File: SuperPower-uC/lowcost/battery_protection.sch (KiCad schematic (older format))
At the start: 0 parts

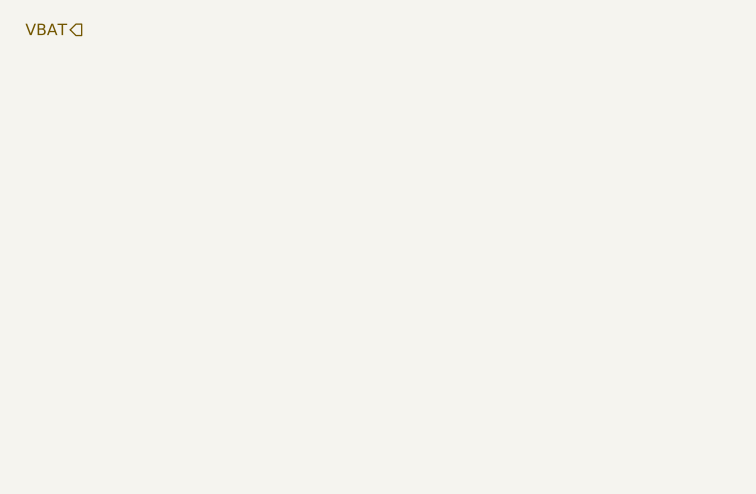
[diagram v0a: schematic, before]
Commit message: added battery protection schematic
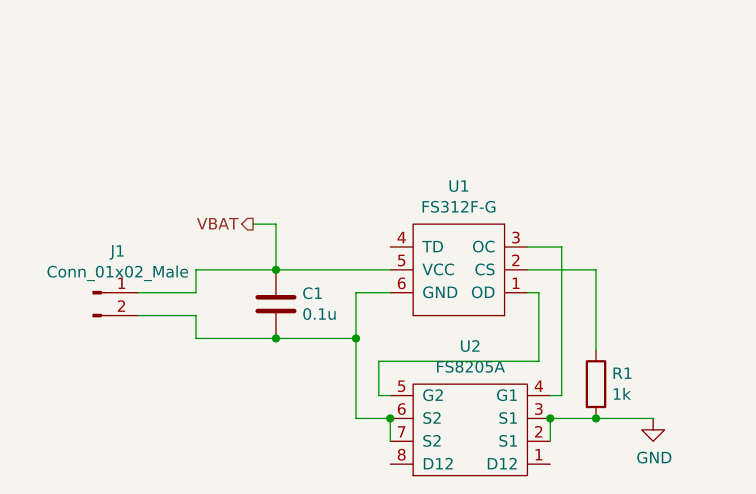
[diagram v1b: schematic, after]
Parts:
- added C1: 0.1u, Capacitor_SMD:C_0603_1608Metric_Pad1.05x0.95mm_HandSolder, symbol Device:C
- added J1: Conn_01x02_Male, Connector_JST:JST_EH_S2B-EH_1x02_P2.50mm_Horizontal, symbol Connector:Conn_01x02_Male
- added R1: 1k, Resistor_SMD:R_0603_1608Metric_Pad1.05x0.95mm_HandSolder, symbol Device:R
- added U1: FS312F-G, Package_TO_SOT_SMD:SOT-23-6_Handsoldering, symbol FS312F-G:FS312F-G
- added U2: FS8205A, Package_SO:TSSOP-8_4.4x3mm_P0.65mm, symbol FS8205A:FS8205A
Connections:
- net VBAT: now also C1.1, J1.1 (Pin_1), U1.5 (VCC)
- new net: U1.1 (OD), U2.5 (G2)
- new net: R1.1, U1.2 (CS)
- new net: U1.3 (OC), U2.4 (G1)
- new net: C1.2, J1.2 (Pin_2), U1.6 (GND), U2.6 (S2), U2.7 (S2)
- new net GND: R1.2, U2.2 (S1), U2.3 (S1)
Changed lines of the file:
@@
 Comment4 ""
 $EndDescr
-Text HLabel 1250 1350 0    50   Output ~ 0
+Text HLabel 2000 2200 0    50   Output ~ 0
 VBAT
+$Comp
+L FS312F-G:FS312F-G U1
+U 1 1 5F7C508D
+P 2900 2500
+F 0 "U1" H 2900 2035 50  0000 C CNN
+F 1 "FS312F-G" H 2900 2126 50  0000 C CNN
+F 2 "Package_TO_SOT_SMD:SOT-23-6_Handsoldering" H 3000 2950 50  0001 C CNN
+F 3 "https://www.ic-fortune.com/upload/Download/FS312F-G-DS-12_EN.pdf" H 2900 2250 50  0001 C CNN
+F 4 " C82736" H 2900 2500 50  0001 C CNN "LCSC"
+	1    2900 2500
+	-1   0    0    1
+$EndComp
+$Comp
+L FS8205A:FS8205A U2
+U 1 1 5F7C57B0
+P 2950 3150
+F 0 "U2" H 2950 2735 50  0000 C CNN
+F 1 "FS8205A" H 2950 2826 50  0000 C CNN
+F 2 "Package_SO:TSSOP-8_4.4x3mm_P0.65mm" H 2950 3450 50  0001 C CNN
+F 3 "https://www.ic-fortune.com/upload/Download/FS8205A-DS-12_EN.pdf" H 2950 3450 50  0001 C CNN
+F 4 " C16052" H 2950 3150 50  0001 C CNN "LCSC"
+	1    2950 3150
+	-1   0    0    1
+$EndComp
+Wire Wire Line
+	2600 2950 2550 2950
+Wire Wire Line
+	2550 2950 2550 2800
+Wire Wire Line
+	2550 2800 3250 2800
+Wire Wire Line
+	3250 2800 3250 2500
+Wire Wire Line
+	3250 2500 3200 2500
+Wire Wire Line
+	3200 2300 3350 2300
+Wire Wire Line
+	3350 2300 3350 2950
+Wire Wire Line
+	3350 2950 3300 2950
+Wire Wire Line
+	2600 3150 2600 3050
+Wire Wire Line
+	2600 3050 2450 3050
+Wire Wire Line
+	2450 2500 2600 2500
+Connection ~ 2600 3050
+Wire Wire Line
+	2600 2400 2100 2400
+Wire Wire Line
+	2450 2700 2100 2700
+Wire Wire Line
+	2000 2200 2100 2200
+Wire Wire Line
+	2100 2200 2100 2400
+Connection ~ 2100 2400
+Wire Wire Line
+	2100 2400 1750 2400
+$Comp
+L Device:R R1
+U 1 1 5F7CFA8D
+P 3500 2900
+F 0 "R1" H 3570 2946 50  0000 L CNN
+F 1 "1k" H 3570 2855 50  0000 L CNN
+F 2 "Resistor_SMD:R_0603_1608Metric_Pad1.05x0.95mm_HandSolder" V 3430 2900 50  0001 C CNN
+F 3 "~" H 3500 2900 50  0001 C CNN
+F 4 "C21190" H 3500 2900 50  0001 C CNN "LCSC"
+	1    3500 2900
+	1    0    0    -1
+$EndComp
+$Comp
+L Device:C C1
+U 1 1 5F7D0298
+P 2100 2550
+F 0 "C1" H 2215 2596 50  0000 L CNN
+F 1 "0.1u" H 2215 2505 50  0000 L CNN
+F 2 "Capacitor_SMD:C_0603_1608Metric_Pad1.05x0.95mm_HandSolder" H 2138 2400 50  0001 C CNN
+F 3 "~" H 2100 2550 50  0001 C CNN
+F 4 "C14858" H 2100 2550 50  0001 C CNN "LCSC"
+	1    2100 2550
+	1    0    0    -1
+$EndComp
+Connection ~ 2100 2700
+Wire Wire Line
+	2100 2700 1750 2700
+Connection ~ 2450 2700
+Wire Wire Line
+	2450 2700 2450 2500
+Wire Wire Line
+	2450 2700 2450 3050
+Wire Wire Line
+	3500 3050 3300 3050
+Wire Wire Line
+	3300 3150 3300 3050
+Connection ~ 3300 3050
+Wire Wire Line
+	3500 2750 3500 2400
+Wire Wire Line
+	3500 2400 3200 2400
+$Comp
+L power:GND #PWR?
+U 1 1 5F7D3A76
+P 3750 3050
+F 0 "#PWR?" H 3750 2800 50  0001 C CNN
+F 1 "GND" H 3755 2877 50  0000 C CNN
+F 2 "" H 3750 3050 50  0001 C CNN
+F 3 "" H 3750 3050 50  0001 C CNN
+	1    3750 3050
+	1    0    0    -1
+$EndComp
+Wire Wire Line
+	3750 3050 3500 3050
+Connection ~ 3500 3050
+$Comp
+L Connector:Conn_01x02_Male J1
+U 1 1 5F7D5382
+P 1300 2500
+F 0 "J1" H 1408 2681 50  0000 C CNN
+F 1 "Conn_01x02_Male" H 1408 2590 50  0000 C CNN
+F 2 "Connector_JST:JST_EH_S2B-EH_1x02_P2.50mm_Horizontal" H 1300 2500 50  0001 C CNN
+F 3 "~" H 1300 2500 50  0001 C CNN
+F 4 "C157931" H 1300 2500 50  0001 C CNN "LCSC"
+	1    1300 2500
+	1    0    0    -1
+$EndComp
+Wire Wire Line
+	1750 2400 1750 2500
+Wire Wire Line
+	1750 2500 1500 2500
+Wire Wire Line
+	1500 2600 1750 2600
+Wire Wire Line
+	1750 2600 1750 2700
 $EndSCHEMATC

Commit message: int pins and charging module
added Interrupt pins to the main sheet and finished the charging module sub sheet (with charger, fuel Gauge and power on int)
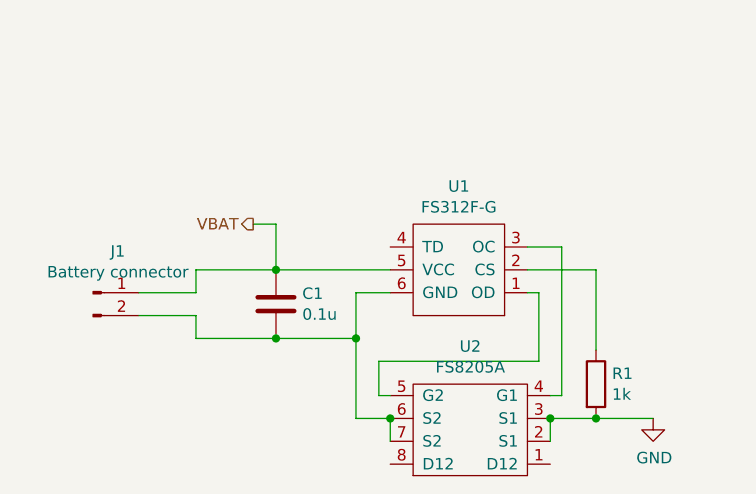
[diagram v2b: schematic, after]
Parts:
- J1: value Conn_01x02_Male -> Battery connector
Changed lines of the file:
@@
 P 1300 2500
 F 0 "J1" H 1408 2681 50  0000 C CNN
-F 1 "Conn_01x02_Male" H 1408 2590 50  0000 C CNN
+F 1 "Battery connector" H 1408 2590 50  0000 C CNN
 F 2 "Connector_JST:JST_EH_S2B-EH_1x02_P2.50mm_Horizontal" H 1300 2500 50  0001 C CNN
 F 3 "~" H 1300 2500 50  0001 C CNN

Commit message: added ftdi and some cleanup
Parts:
- U1: LCSC C82736 -> C82736
- U2: LCSC C16052 -> C16052
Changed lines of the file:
@@
 F 2 "Package_TO_SOT_SMD:SOT-23-6_Handsoldering" H 3000 2950 50  0001 C CNN
 F 3 "https://www.ic-fortune.com/upload/Download/FS312F-G-DS-12_EN.pdf" H 2900 2250 50  0001 C CNN
-F 4 " C82736" H 2900 2500 50  0001 C CNN "LCSC"
+F 4 "C82736" H 2900 2500 50  0001 C CNN "LCSC"
 	1    2900 2500
 	-1   0    0    1
@@
 F 2 "Package_SO:TSSOP-8_4.4x3mm_P0.65mm" H 2950 3450 50  0001 C CNN
 F 3 "https://www.ic-fortune.com/upload/Download/FS8205A-DS-12_EN.pdf" H 2950 3450 50  0001 C CNN
-F 4 " C16052" H 2950 3150 50  0001 C CNN "LCSC"
+F 4 "C16052" H 2950 3150 50  0001 C CNN "LCSC"
 	1    2950 3150
 	-1   0    0    1
@@
 F 1 "Battery connector" H 1408 2590 50  0000 C CNN
 F 2 "Connector_JST:JST_EH_S2B-EH_1x02_P2.50mm_Horizontal" H 1300 2500 50  0001 C CNN
-F 3 "~" H 1300 2500 50  0001 C CNN
+F 3 "https://datasheet.lcsc.com/szlcsc/1811051822_JST-Sales-America-S2B-XH-A-LF-SN_C157931.pdf" H 1300 2500 50  0001 C CNN
 F 4 "C157931" H 1300 2500 50  0001 C CNN "LCSC"
 	1    1300 2500

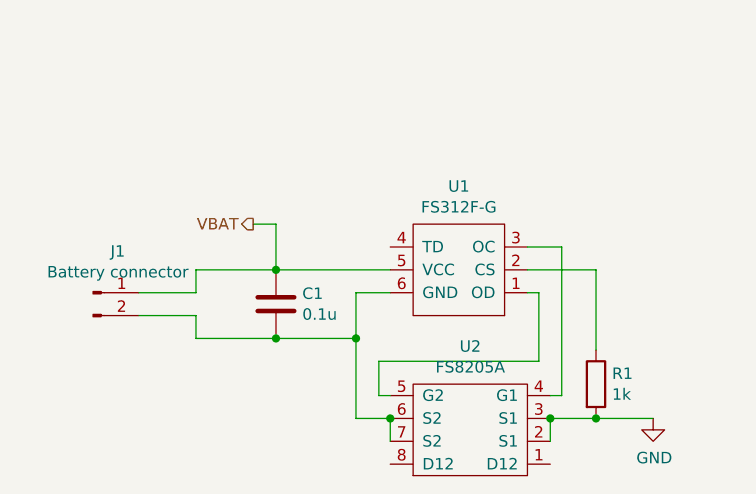
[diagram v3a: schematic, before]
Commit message: fixed mentioned issues and swapped micro usb with usb c
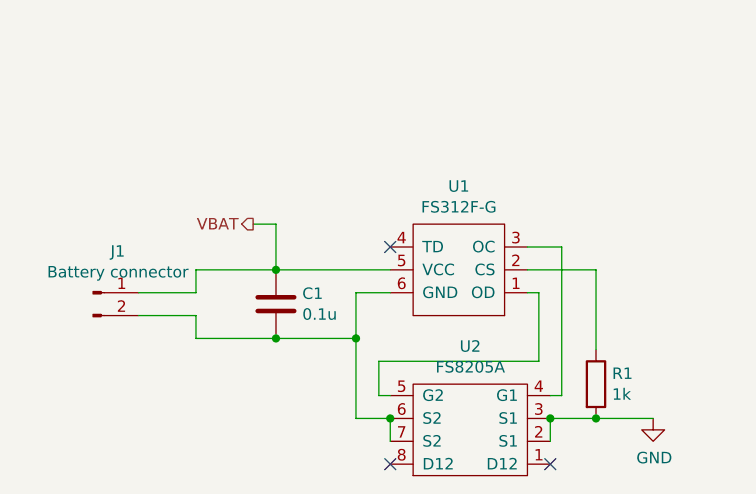
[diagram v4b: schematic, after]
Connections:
- no-connect marks 0 -> 3
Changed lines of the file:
@@
 Wire Wire Line
 	1750 2600 1750 2700
+NoConn ~ 2600 3250
+NoConn ~ 3300 3250
+NoConn ~ 2600 2300
 $EndSCHEMATC

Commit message: io expander, rtc cirquit, i2c pullup...
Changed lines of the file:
@@
 Comment4 ""
 $EndDescr
-Text HLabel 2000 2200 0    50   Output ~ 0
+Text HLabel 2000 2200 0    50   BiDi ~ 0
 VBAT
 $Comp

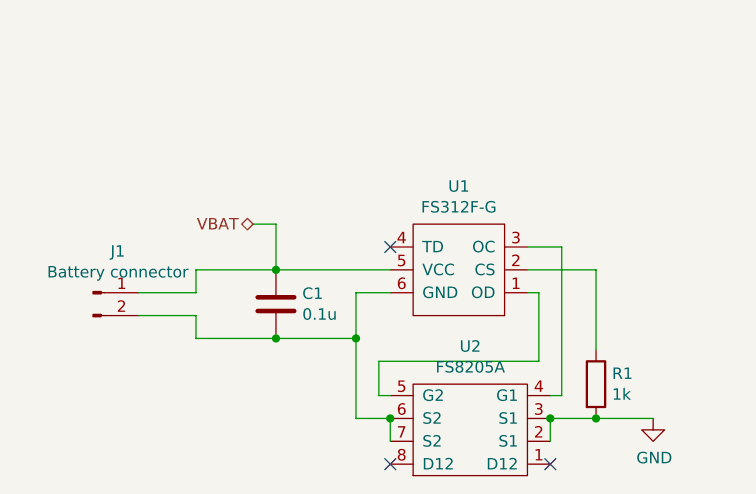
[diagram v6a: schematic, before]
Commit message: fixed erc errors
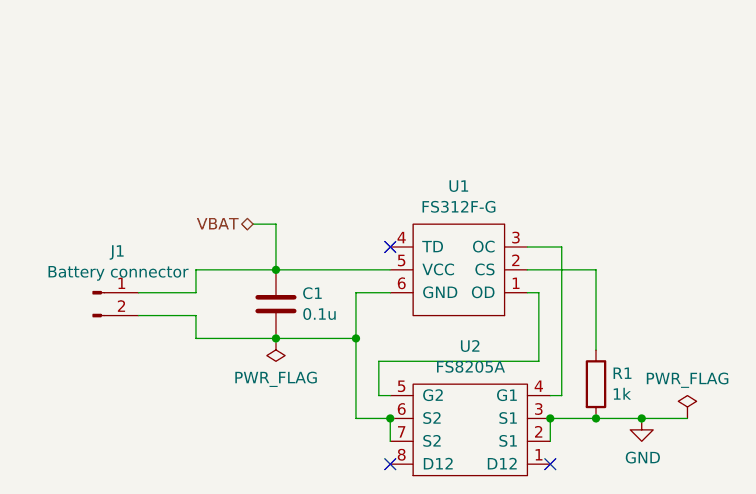
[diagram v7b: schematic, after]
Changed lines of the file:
@@
 L power:GND #PWR0101
 U 1 1 5F7D3A76
-P 3750 3050
-F 0 "#PWR0101" H 3750 2800 50  0001 C CNN
-F 1 "GND" H 3755 2877 50  0000 C CNN
-F 2 "" H 3750 3050 50  0001 C CNN
-F 3 "" H 3750 3050 50  0001 C CNN
-	1    3750 3050
+P 3700 3050
+F 0 "#PWR0101" H 3700 2800 50  0001 C CNN
+F 1 "GND" H 3705 2877 50  0000 C CNN
+F 2 "" H 3700 3050 50  0001 C CNN
+F 3 "" H 3700 3050 50  0001 C CNN
+	1    3700 3050
 	1    0    0    -1
 $EndComp
-Wire Wire Line
-	3750 3050 3500 3050
 Connection ~ 3500 3050
 $Comp
@@
 NoConn ~ 3300 3250
 NoConn ~ 2600 2300
+Wire Wire Line
+	3700 3050 3500 3050
+$Comp
+L power:PWR_FLAG #FLG0102
+U 1 1 5F858ADE
+P 2100 2700
+F 0 "#FLG0102" H 2100 2775 50  0001 C CNN
+F 1 "PWR_FLAG" H 2100 2873 50  0000 C CNN
+F 2 "" H 2100 2700 50  0001 C CNN
+F 3 "~" H 2100 2700 50  0001 C CNN
+	1    2100 2700
+	-1   0    0    1
+$EndComp
+$Comp
+L power:PWR_FLAG #FLG0103
+U 1 1 5F859212
+P 3900 3050
+F 0 "#FLG0103" H 3900 3125 50  0001 C CNN
+F 1 "PWR_FLAG" H 3900 3223 50  0000 C CNN
+F 2 "" H 3900 3050 50  0001 C CNN
+F 3 "~" H 3900 3050 50  0001 C CNN
+	1    3900 3050
+	1    0    0    -1
+$EndComp
+Wire Wire Line
+	3700 3050 3900 3050
+Connection ~ 3700 3050
 $EndSCHEMATC

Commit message: design rule optimisation
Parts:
- C1: value 0.1u -> 0.1µF
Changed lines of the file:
@@
 P 2100 2550
 F 0 "C1" H 2215 2596 50  0000 L CNN
-F 1 "0.1u" H 2215 2505 50  0000 L CNN
+F 1 "0.1µF" H 2215 2505 50  0000 L CNN
 F 2 "Capacitor_SMD:C_0603_1608Metric_Pad1.05x0.95mm_HandSolder" H 2138 2400 50  0001 C CNN
 F 3 "~" H 2100 2550 50  0001 C CNN
